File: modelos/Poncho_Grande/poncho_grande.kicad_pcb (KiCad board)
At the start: 2 copper layers, 85.7 x 137.2 mm, 25 parts, among them P1 CONN_02X20, P10 CONN_01X20, P11 CONN_01X20, P12 CONN_01X06, P13 CONN_01X06, P14 CONN_02X12, P15 CONN_02X12, P16 CONN_02X12, P17 CONN_02X12, P18 CONN_01X12, P19 CONN_01X12, P2 CONN_01X20, P20 CONN_01X12, P21 CONN_01X12, P3 CONN_02X20, P4 CONN_02X20, P5 CONN_01X19, P6 CONN_02X20, P7 CONN_01X20, P8 CONN_02X20, P9 CONN_02X20

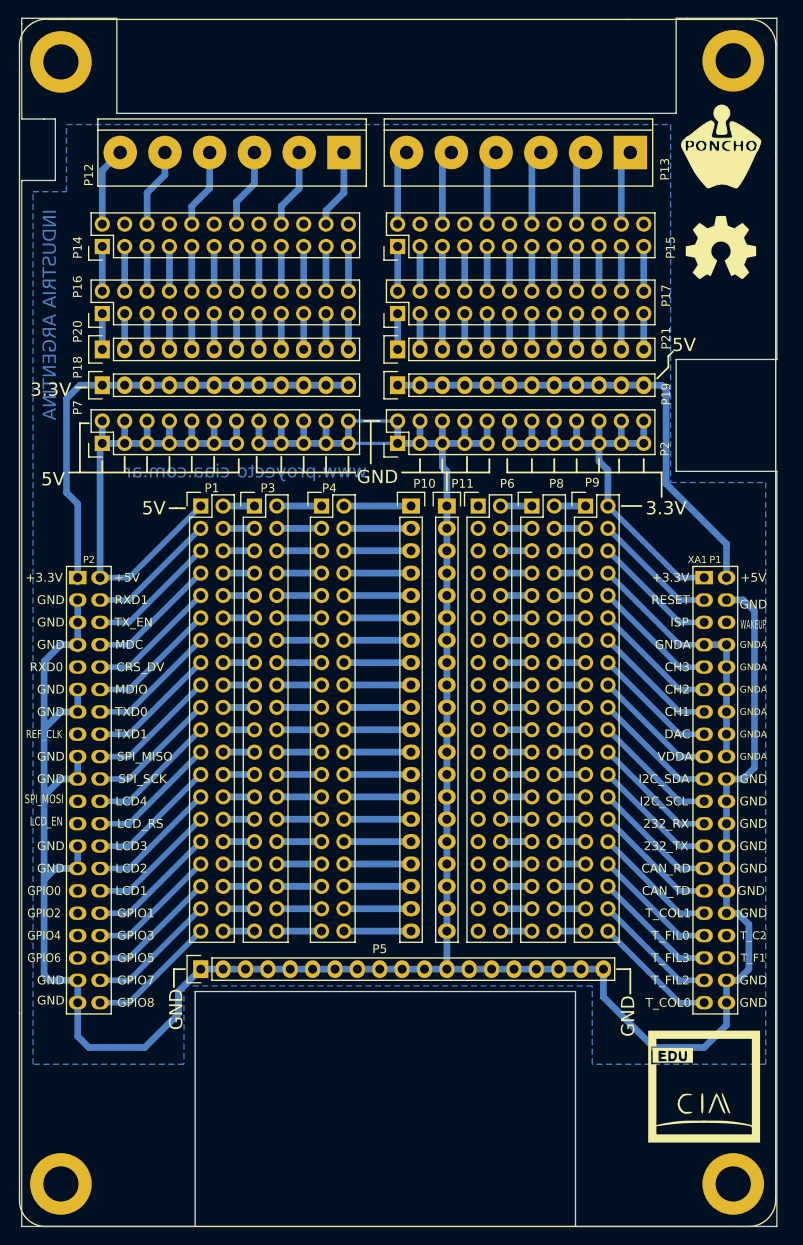
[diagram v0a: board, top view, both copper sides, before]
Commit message: * Agrego leyendas e instructivos de uso en el esquema y el PCB. Agrego carpeta ./doc modelo.
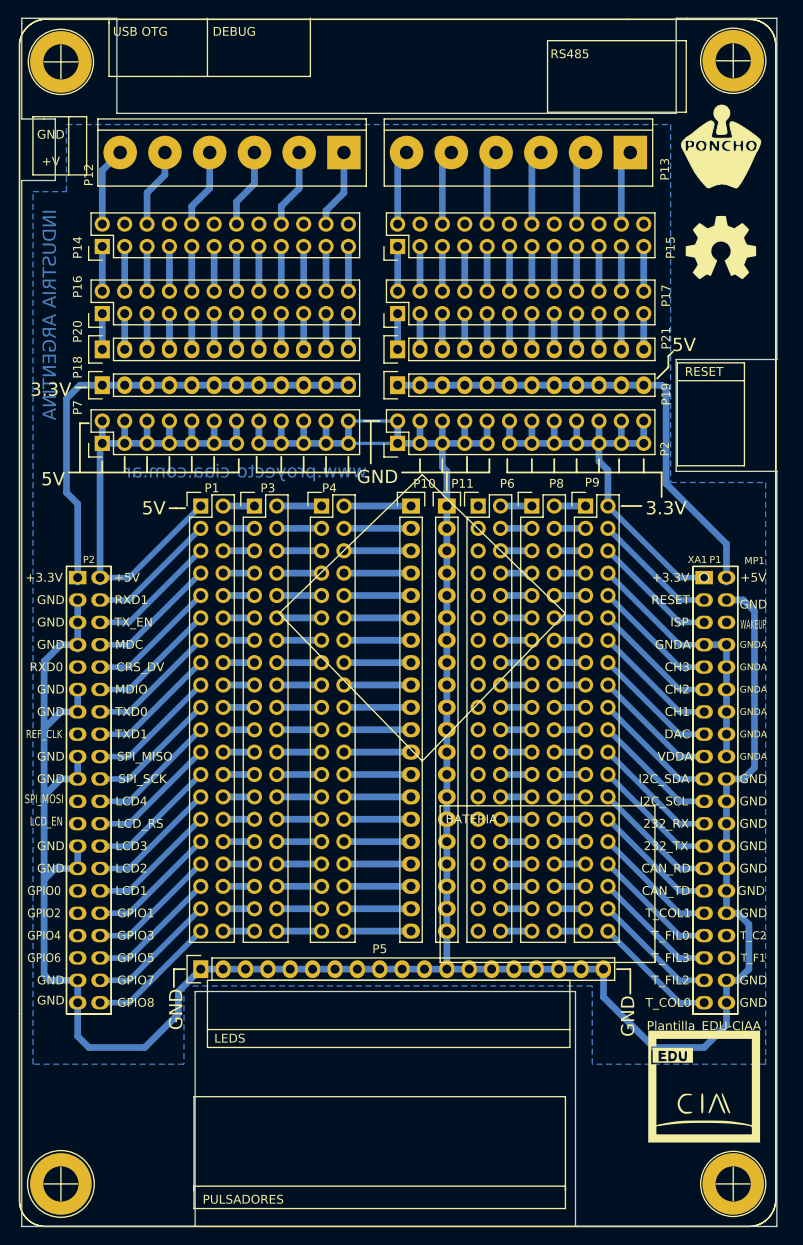
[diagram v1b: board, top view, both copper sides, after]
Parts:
- added MP1: Plantilla_EDU-CIAA, Poncho_Esqueleto:Plantilla_EDU-CIAA, F.Cu at (151.1, 88.9)
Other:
- board text added: "Borrar (Footprint MP1) la Plantilla-EDU-CIAA al finalizar el posicionamiento y definido el borde de PCB."
- board text added: "Colocar código de Poncho en cobre, serigrafía y rótulo."
- board text added: "Editar el rótulo"
- board text added: "Editar el stackup para reflejar cantidad de capas, si se han realizado cálculos de impedancia o si es relevante para el funcionamiento."
- board text added: "Para un diseño nuevo luego de modificar el esquemático: 1)Seleccionar el bloque del PCB y cotas. (click-drag-release). 2)Opción de borrar bloque (Botón derecho). 3)Marcar todo menos locked footprints (MP1 y XA1) 4) Aceptar. 5) Volver a cargar el netlist."
- board text added: "STACK-UP PCB de simple faz Sin requisitos de Stackup"
- board text removed: "Borrar la Plantilla-EDU-CIAA al finalizar el posicionamiento y el borde de PCB."
